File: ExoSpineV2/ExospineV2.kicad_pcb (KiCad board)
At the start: 2 copper layers, 80.4 x 72.4 mm, 55 parts, among them J1 GPIO, J11 JST PH 3pin, J12 2.54mm 4pin, J13 JST PH 4pin, J15 JST PH 3pin, J16 JST PH 3pin, J2 Screw Terminal 2pin 5mm, J21 JST PH 2pin, J22 JST PH 2pin, J23 JST PH 2pin, J24 JST PH 2pin, J31 JST PH 3pin, J32 JST PH 3pin, J33 JST PH 3pin, J34 JST PH 3pin, J35 JST PH 3pin, J36 JST PH 3pin, J41 JST PH 2pin, J42 JST PH 3pin, J43 JST PH 3pin, J51 JST PH 4pin, J52 JST PH 3pin, J53 JST PH 4pin, J54 JST PH 3pin, J55 JST PH 4pin, J56 JST PH 3pin, J6 JST PH 2pin, U1 MCP3008-I/SL, U2 74HC00D,653, U3 74HC00D,653

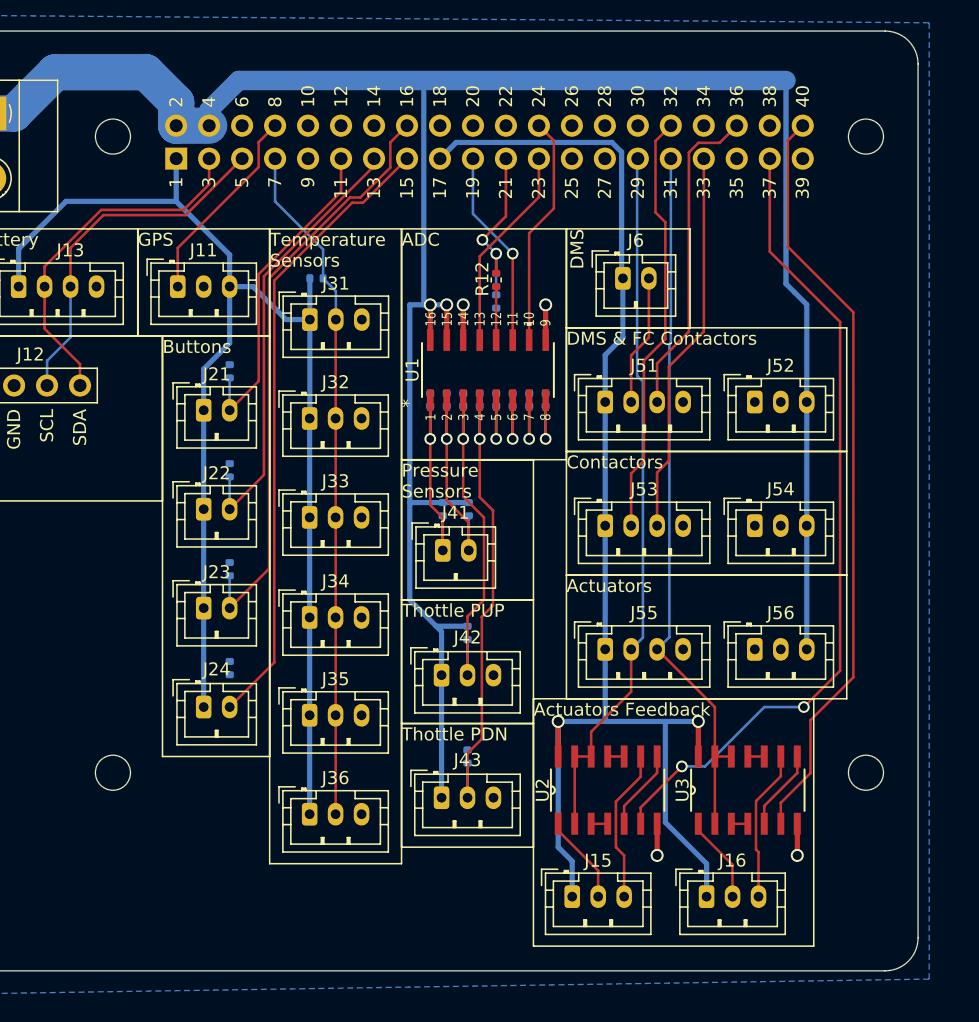
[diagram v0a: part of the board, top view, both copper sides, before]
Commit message: added a 2 relay module
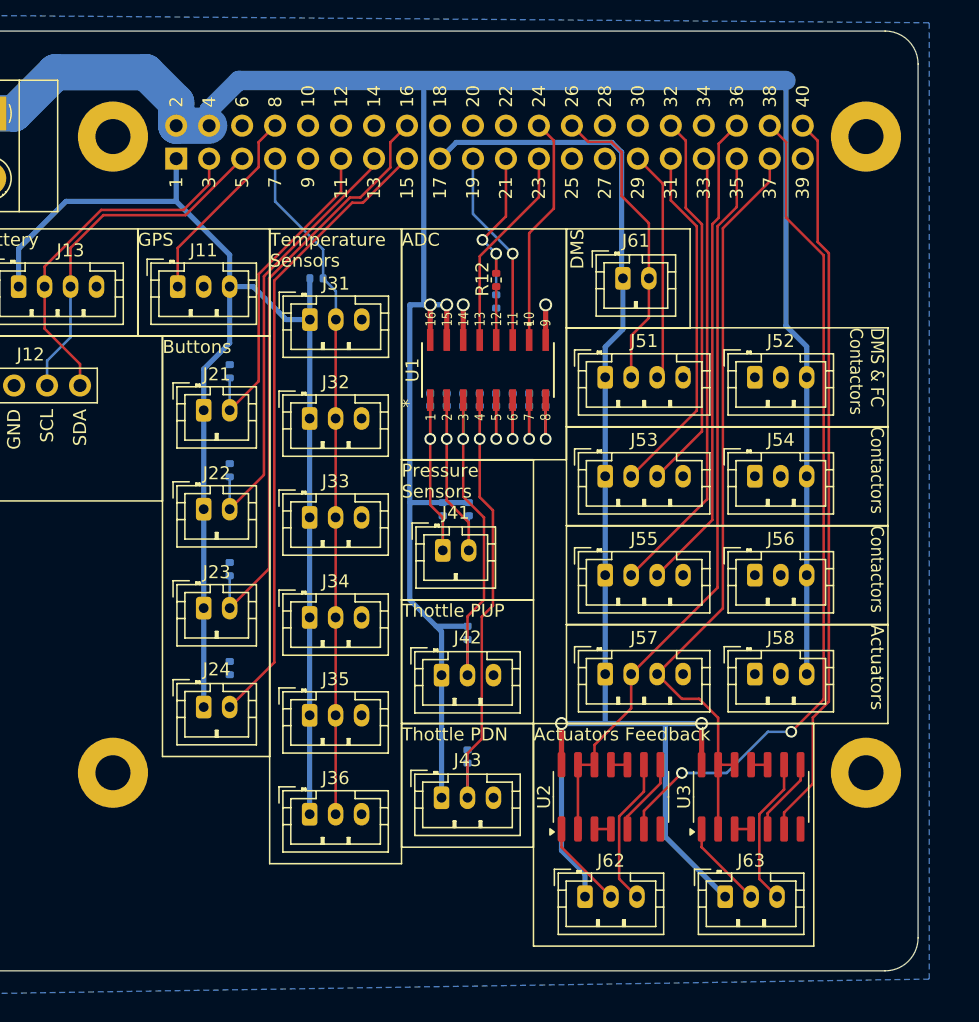
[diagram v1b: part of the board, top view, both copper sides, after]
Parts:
- removed MH1, MH2, MH3, MH4: MountingHole_2.7mm_M2.5, MountingHole:MountingHole_2.7mm_M2.5
- added J3: Mounting Hole 2.7mm, MountingHole:MountingHole_2.7mm_Pad, F.Cu at (103.5, 47.5)
- added J4: Mounting Hole 2.7mm, MountingHole:MountingHole_2.7mm_Pad, F.Cu at (161.5, 47.5)
- added J5: Mounting Hole 2.7mm, MountingHole:MountingHole_2.7mm_Pad, F.Cu at (103.5, 96.5)
- added J57: JST PH 4pin, Connector_JST:JST_PH_B4B-PH-K_1x04_P2.00mm_Vertical, F.Cu at (141.4, 88.9)
- added J58: JST PH 3pin, Connector_JST:JST_PH_B3B-PH-K_1x03_P2.00mm_Vertical, F.Cu at (152.9, 88.9)
- added J6: Mounting Hole 2.7mm, MountingHole:MountingHole_2.7mm_Pad, F.Cu at (161.5, 96.5)
- U2, U3: footprint ExoSpineV2:SOIC127P600X175-14N_74HC00D653 -> Package_SO:SOIC-14_3.9x8.7mm_P1.27mm
- moved J55 5.72 mm to (141.4, 81.3)
- moved J56 5.72 mm to (152.9, 81.3)
- moved J53 3.81 mm to (141.4, 73.7)
- moved J54 3.81 mm to (152.9, 73.7)
- moved J51 1.90 mm to (141.4, 66.0)
- moved J52 1.90 mm to (152.9, 66.0)
- moved J63 1.43 mm to (150.7, 106.0)
- moved J62 0.98 mm to (139.9, 106.0)
- moved U2 0.58 mm to (141.9, 98.4)
- moved U3 0.58 mm to (152.7, 98.4)
- renumbered J6 to J61, J15 to J62, J16 to J63
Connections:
- J51 pad 2: /DMS -> /GPIO7/SPI0.CE1
- J51 pad 3: /GPIO16 -> /GPIO5
- J53 pad 2: /GPIO12/PWM0 -> /GPIO6
- J53 pad 3: /GPIO13/PWM1 -> /GPIO12/PWM0
- J55 pad 2: /GPIO5 -> /GPIO13/PWM1
- J55 pad 3: /GPIO6 -> /GPIO16
- J61 pad 2: /DMS -> /GPIO7/SPI0.CE1
- U2 pad 12: /GPIO5 -> /GPIO19/PCM.FS
- U2 pad 13: /GPIO5 -> /GPIO19/PCM.FS
- U2 pad 2: /GPIO5 -> /GPIO19/PCM.FS
- U2 pad 6: /GPIO26 -> /GPIO20/PCM.DIN
- U3 pad 12: /GPIO6 -> /GPIO26
- U3 pad 13: /GPIO6 -> /GPIO26
- U3 pad 2: /GPIO6 -> /GPIO26
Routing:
- net /GPIO20/PCM.DIN: track 0.00 -> 64.7 mm, vias 0 -> 2
- net /GPIO19/PCM.FS: track 0.00 -> 57.4 mm
- net /GPIO5: track 54.4 -> 17.9 mm
- net /GPIO6: track 54.8 -> 27.4 mm
- net /GPIO7/SPI0.CE1: track 0.00 -> 23.5 mm
- net /GPIO16: track 24.8 -> 37.2 mm
- net /DMS: track 10.1 -> 0.00 mm
- net GND: track 11.0 -> 6.08 mm, vias 4 -> 2
- net /GPIO13/PWM1: track 29.8 -> 34.6 mm
- net /GPIO26: track 62.7 -> 59.2 mm, vias 2 -> 0
- net /GPIO12/PWM0: track 32.7 -> 29.4 mm
- net /GPIO21/PCM.DOUT: track 58.7 -> 56.4 mm
- net +3.3V: track 214.1 -> 216.0 mm
- net +5V: track 183.5 -> 185.4 mm
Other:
- board text removed: "CAMERA (OPTIONAL)"
- board text removed: "DISPLAY (OPTIONAL)"
- board text removed: "Extend PCB edge 0.5mm if using SMT header"
- board text removed: "PoE"

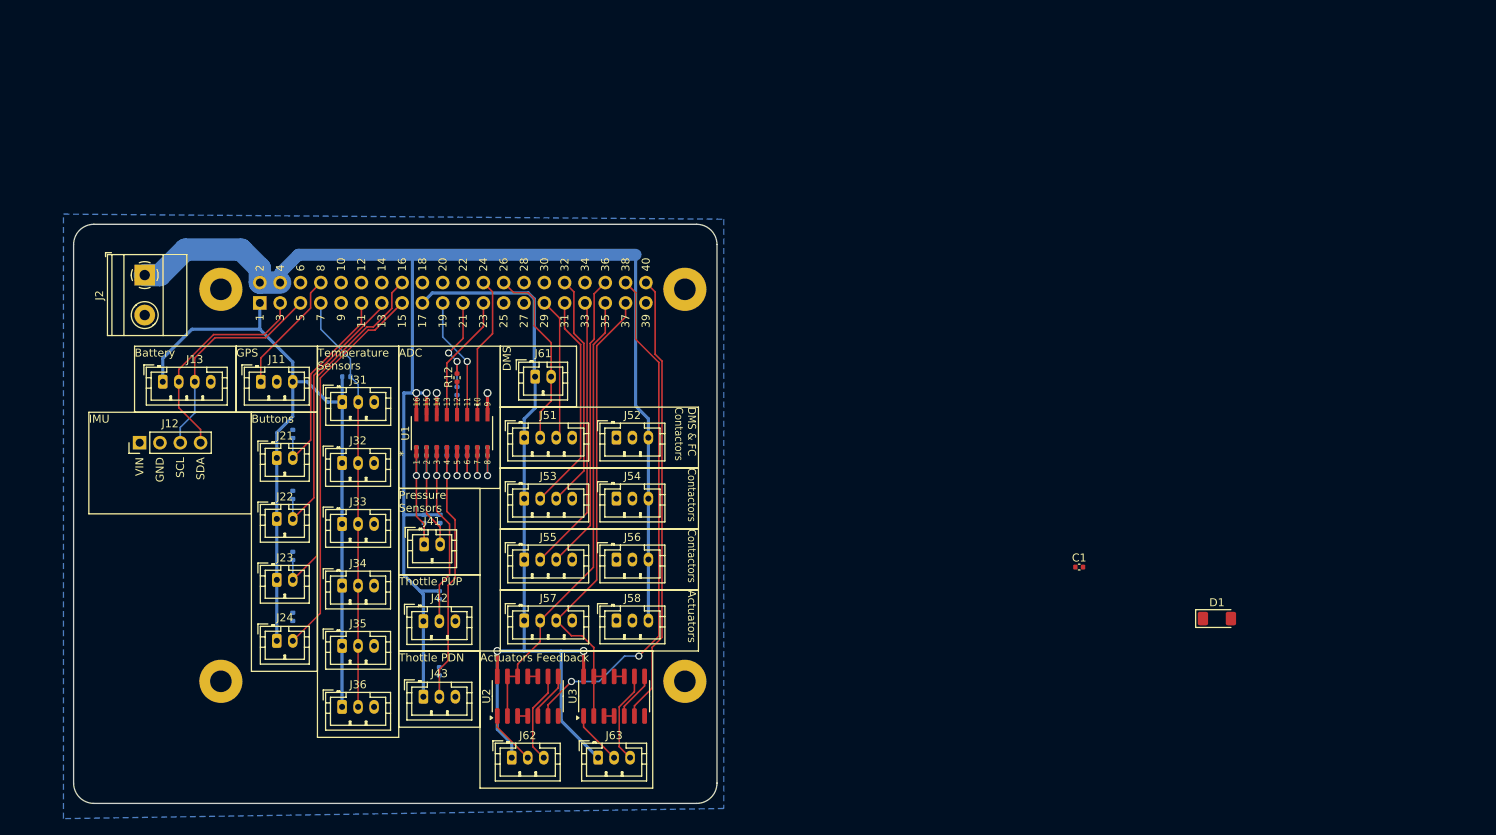
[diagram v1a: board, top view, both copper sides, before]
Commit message: removed Throttle circuits (pull-up & pull-down)
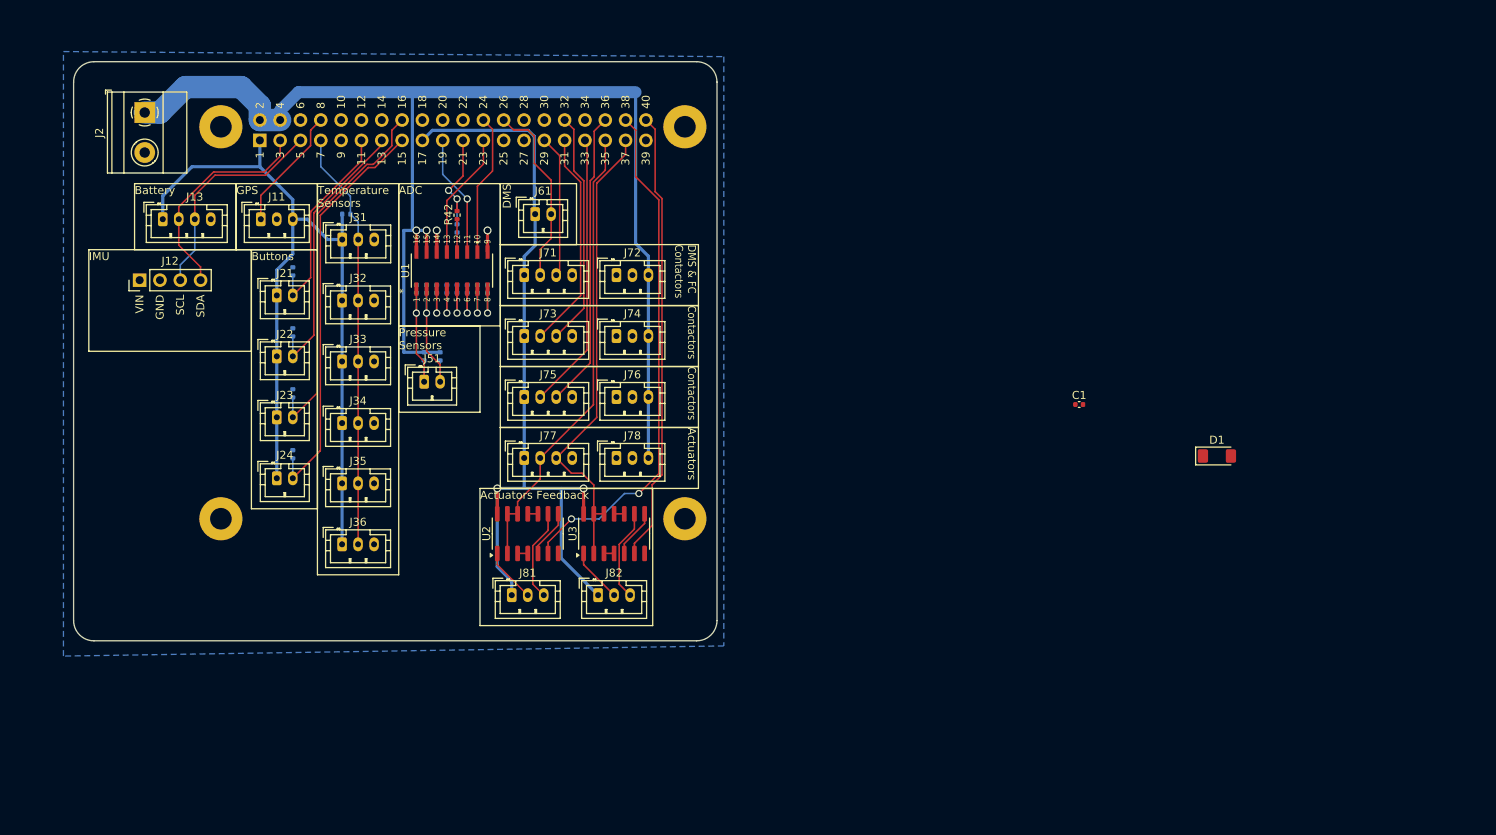
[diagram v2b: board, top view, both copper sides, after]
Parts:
- removed J42, J43: JST PH 3pin, Connector_JST:JST_PH_B3B-PH-K_1x03_P2.00mm_Vertical
- removed R43, R44: 10k, Resistor_SMD:R_0402_1005Metric
- moved D1 20.3 mm to (228.0, 68.3)
- moved J34 20.3 mm to (118.7, 64.2)
- moved J35 20.3 mm to (118.7, 71.8)
- moved J71 20.3 mm to (141.4, 45.7)
- moved J72 20.3 mm to (152.9, 45.7)
- moved J77 20.3 mm to (141.4, 68.6)
- moved J78 20.3 mm to (152.9, 68.6)
- moved J81 20.3 mm to (139.9, 85.7)
- moved J82 20.3 mm to (150.7, 85.7)
- moved J1 20.3 mm to (108.4, 28.9)
- moved C1 20.3 mm to (210.8, 61.9)
- moved J11 20.3 mm to (108.5, 38.7)
- moved J12 20.3 mm to (93.3, 46.4)
- moved J13 20.3 mm to (96.2, 38.7)
- moved J2 20.3 mm to (94.0, 25.4)
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- renumbered C3 to C41, C4 to C42, C5 to C43, C6 to C44, C7 to C45, C8 to C46, C9 to C47, C10 to C48, J41 to J51, J51 to J71, J52 to J72, J53 to J73, J54 to J74, J55 to J75, J56 to J76, J57 to J77, J58 to J78, J62 to J81, J63 to J82, R13 to R41, R12 to R42, R41 to R51, R42 to R52
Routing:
- net /MCP3008.CH3: track 37.1 -> 5.54 mm
- net +5V: track 185.4 -> 159.3 mm
- net /MCP3008.CH2: track 27.7 -> 5.54 mm
- net /GPIO22: track 48.4 -> 50.9 mm
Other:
- outline, holes or cut-outs redrawn
- board text removed: "Thottle PDN"
- board text removed: "Thottle PUP"

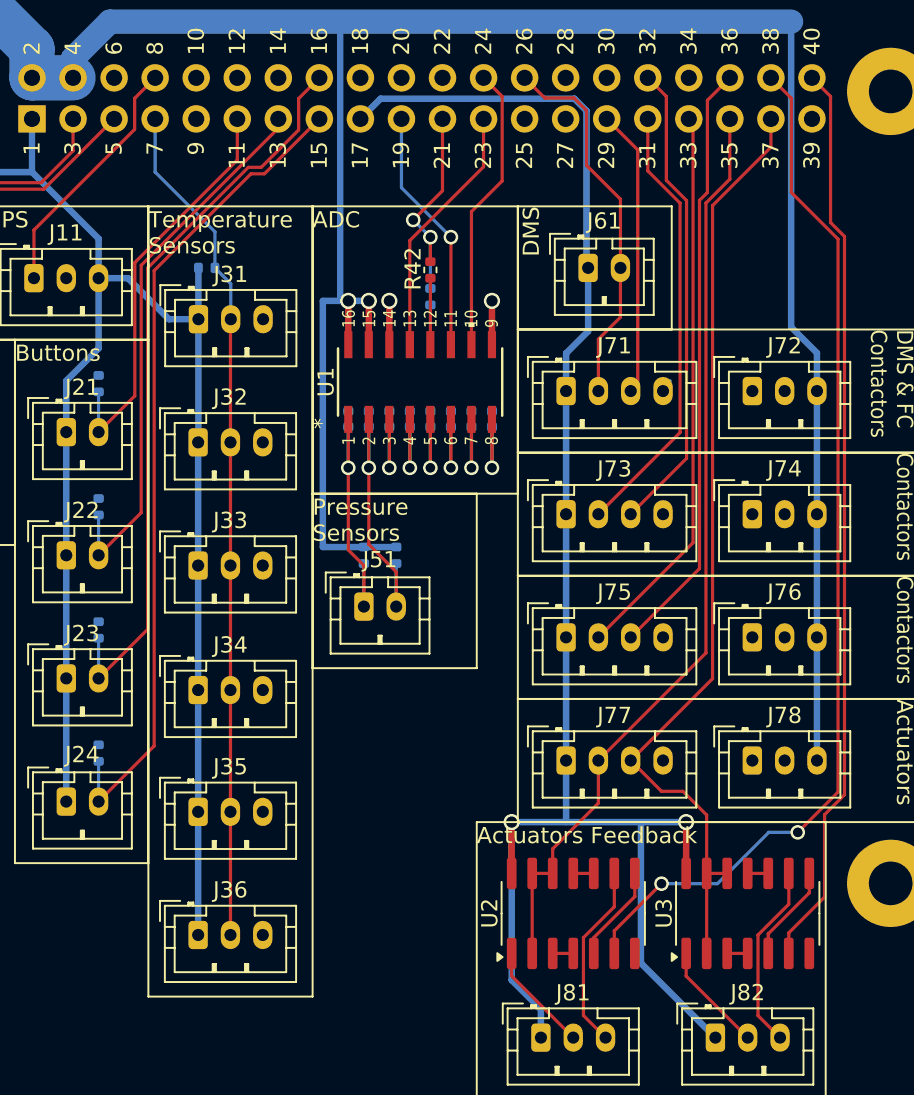
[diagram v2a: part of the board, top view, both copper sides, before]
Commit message: updated footprints
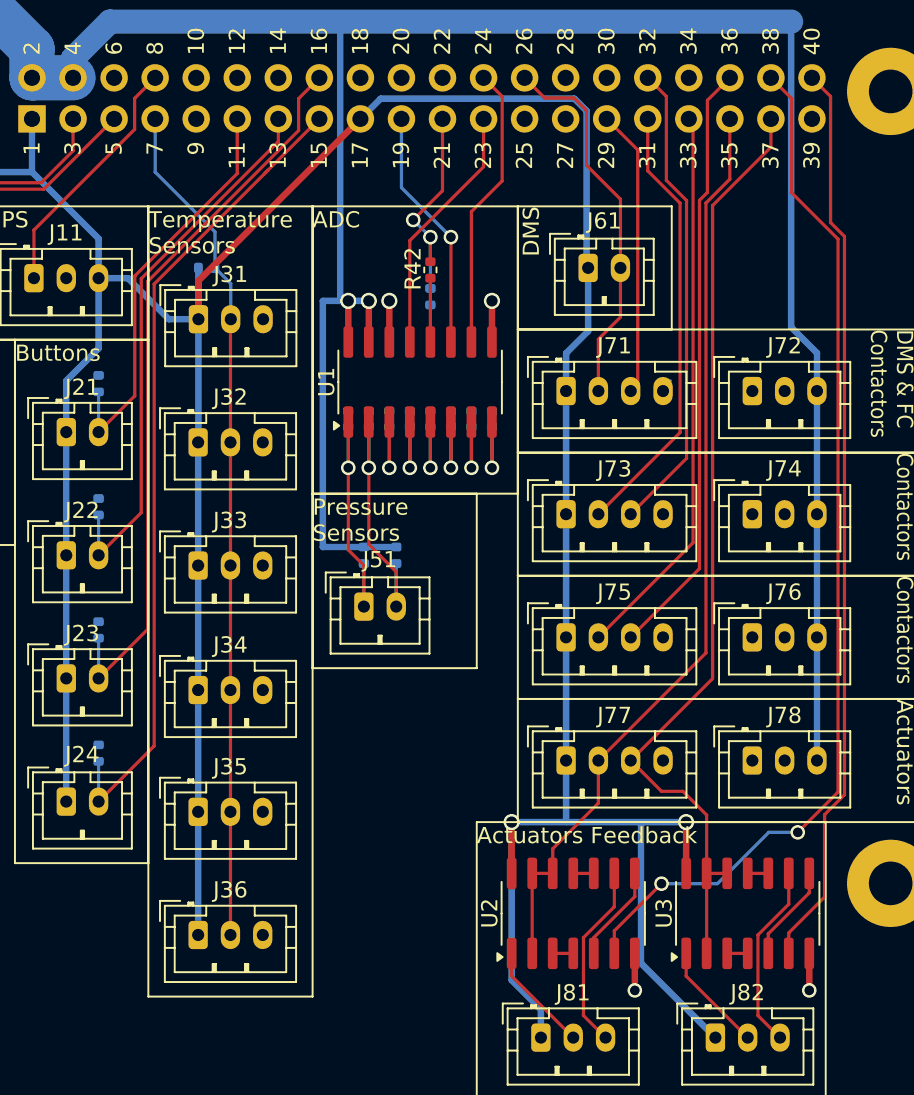
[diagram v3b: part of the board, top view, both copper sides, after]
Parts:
- U1: footprint MCP-3008 MCP3008-I/SL:SOIC16-N_MC_MCH-L -> Package_SO:SOIC-16_3.9x9.9mm_P1.27mm
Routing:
- net +3.3V: track 216.0 -> 232.6 mm
- net GND: track 6.08 -> 10.3 mm, vias 2 -> 4
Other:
- board text removed: "1 2 3 4 5 6 7 8"
- board text removed: "16 15 14 13 12 11 10 9"

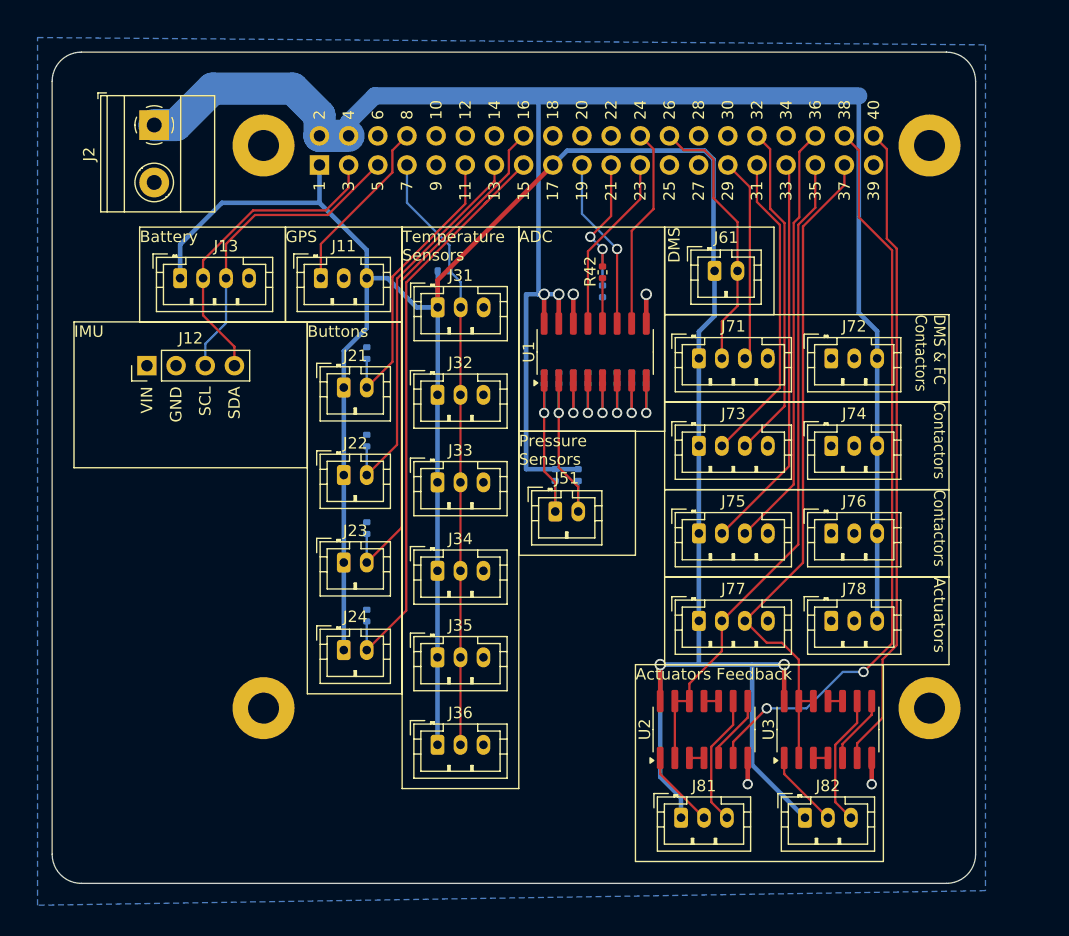
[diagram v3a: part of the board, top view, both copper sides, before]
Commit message: added power plane
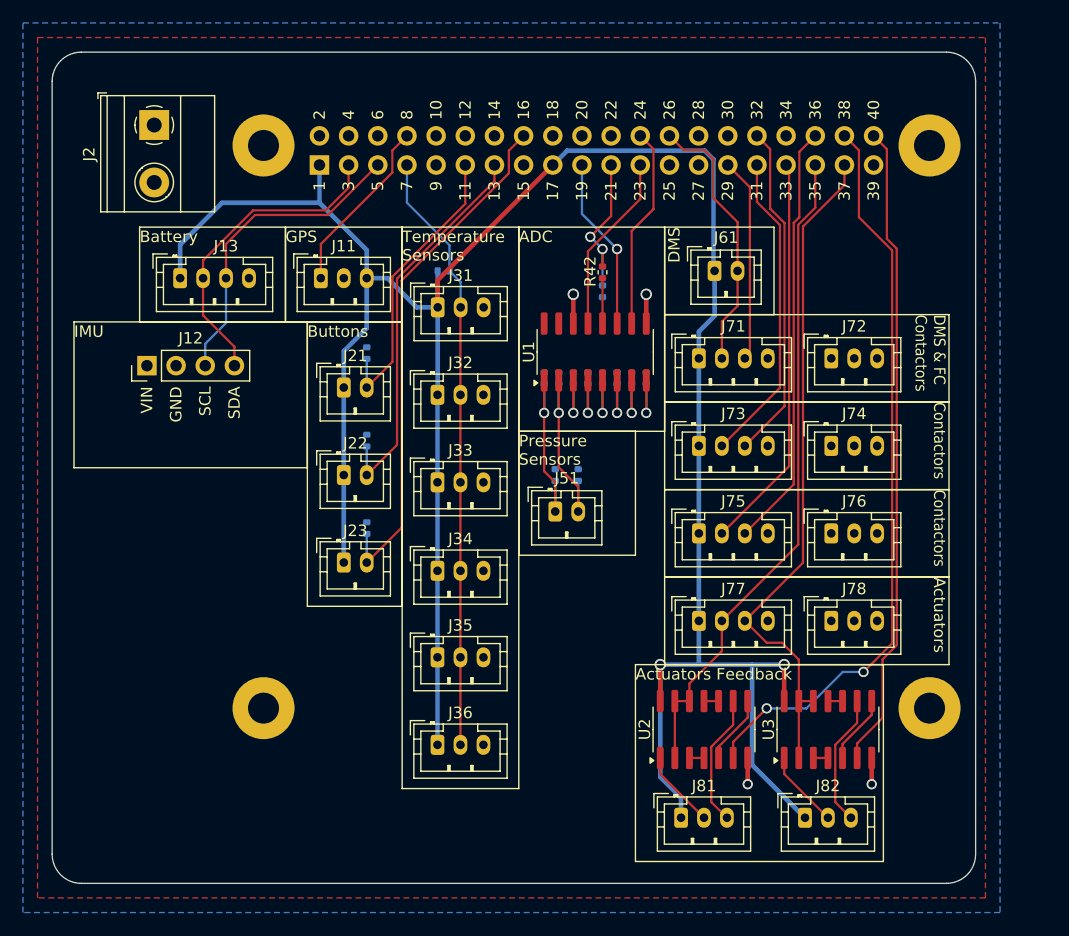
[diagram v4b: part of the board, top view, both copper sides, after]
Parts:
- removed J24: JST PH 2pin, Connector_JST:JST_PH_B2B-PH-K_1x02_P2.00mm_Vertical
- removed R24: 10k, Resistor_SMD:R_0402_1005Metric
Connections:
- J2 pad 1: +5V -> Net-(J2-Pin_1)
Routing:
- net +5V: track 158.9 -> 0.00 mm, vias 2 -> 0
- net /GPIO22: track 50.7 -> 0.00 mm
- net +3.3V: track 232.6 -> 225.0 mm
- added copper zone on F.Cu, net +5V
